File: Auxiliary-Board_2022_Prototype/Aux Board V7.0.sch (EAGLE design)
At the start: 68 parts, among them CON11 1X01, CON12 1X01, CON13 1X01, CON14 1X01, CON15 1X01, CON16 1X01, CON17 1X01, CON18 1X01, CON5 1X01, CON8 1X01, IC1 RS232-TTL_MAX232E

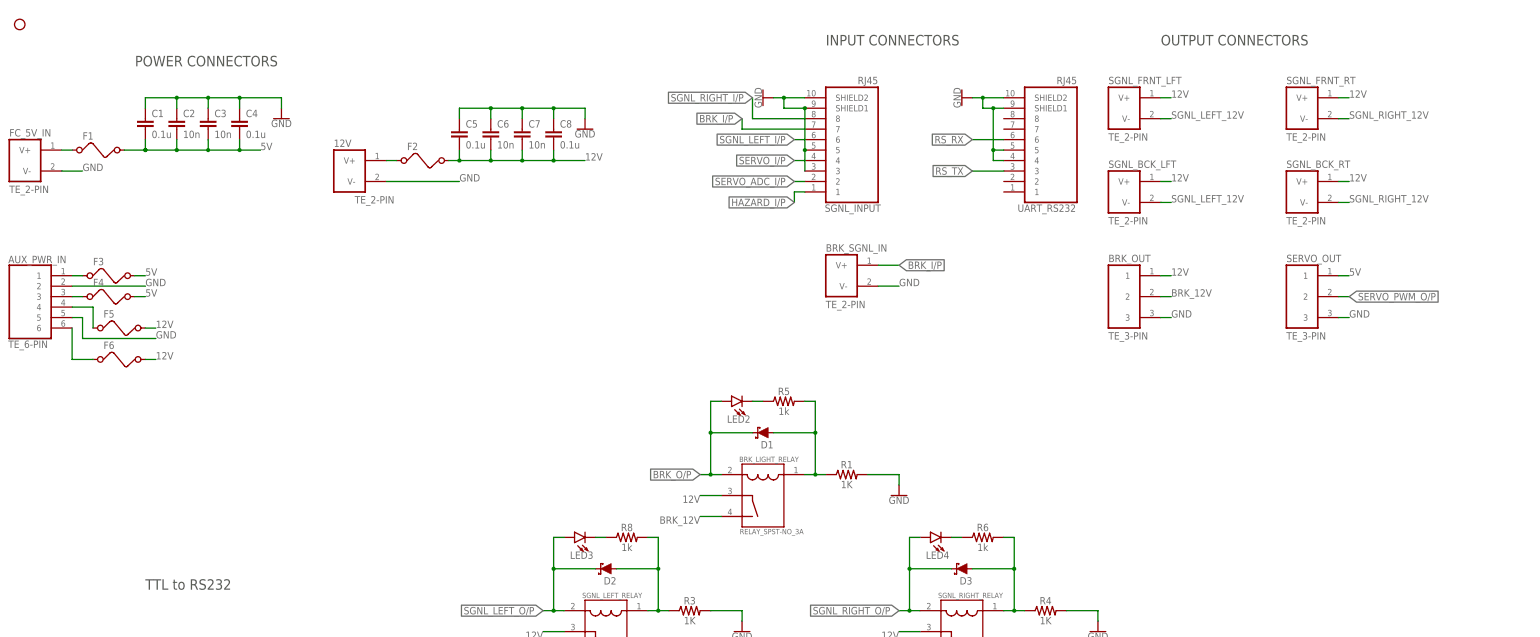
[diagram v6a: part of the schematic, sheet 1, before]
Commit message: feat: connect fuses and power LEDs on board, switch RS232 connector to RJ45 that supports LEDs
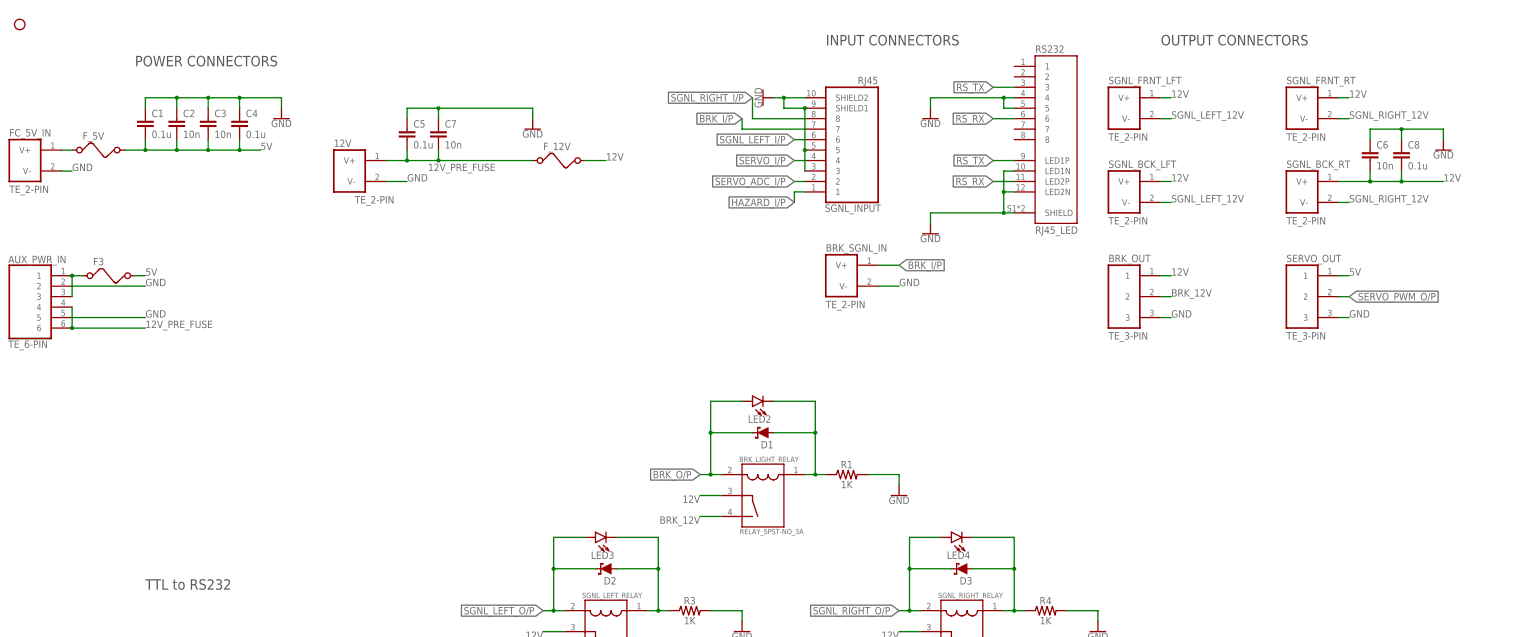
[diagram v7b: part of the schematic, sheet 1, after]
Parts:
- removed F2, F4, F5, F6: (no value), EcoCar-Fuses-Protection:FUSE_1210
- removed R5, R6, R8: 1k, EcoCar-Passives:RESISTOR_0805
- removed UART_RS232: RJ45, EcoCar-Connectors:RJ45
- added F_12V: (no value), EcoCar-Fuses-Protection:FUSE_1210
- added RS232: RJ45_LED, EcoCar-Connectors:RJ45_LED
- renumbered F1 to F_5V
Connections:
- removed net N$30: LED2.C, R5.1
- removed net N$31: LED4.C, R6.1
- removed net N$32: LED3.C, R8.1
- removed net N$35: 12V.V+, F2.1
- removed net N$37: AUX_PWR_IN.3, F4.1
- new net 12V_PRE_FUSE: 12V.V+, AUX_PWR_IN.4, AUX_PWR_IN.6, C5.2, C7.2, F_12V.1
- net 12V: now also F_12V.2; no longer AUX_PWR_IN.4, AUX_PWR_IN.6, C5.2, C7.2, F2.2, F5.1, F5.2, F6.1, F6.2
- net 5V: no longer F4.2
- net GND: now also RS232.4, RS232.5, RS232.LED1N, RS232.LED2N, RS232.SHIELD; no longer UART_RS232.4, UART_RS232.5, UART_RS232.SHIELD1, UART_RS232.SHIELD2
- net N$1: now also LED2.C; no longer R5.2
- net N$13: now also LED3.C; no longer R8.2
- net N$14: now also LED4.C; no longer R6.2
- net N$36: now also AUX_PWR_IN.3
- net RS_RX: now also RS232.6, RS232.LED2P; no longer UART_RS232.6
- net RS_TX: now also RS232.3, RS232.LED1P; no longer UART_RS232.3
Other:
- moved on the sheet: C5, C6, C7, C8, LED2, LED3, LED4

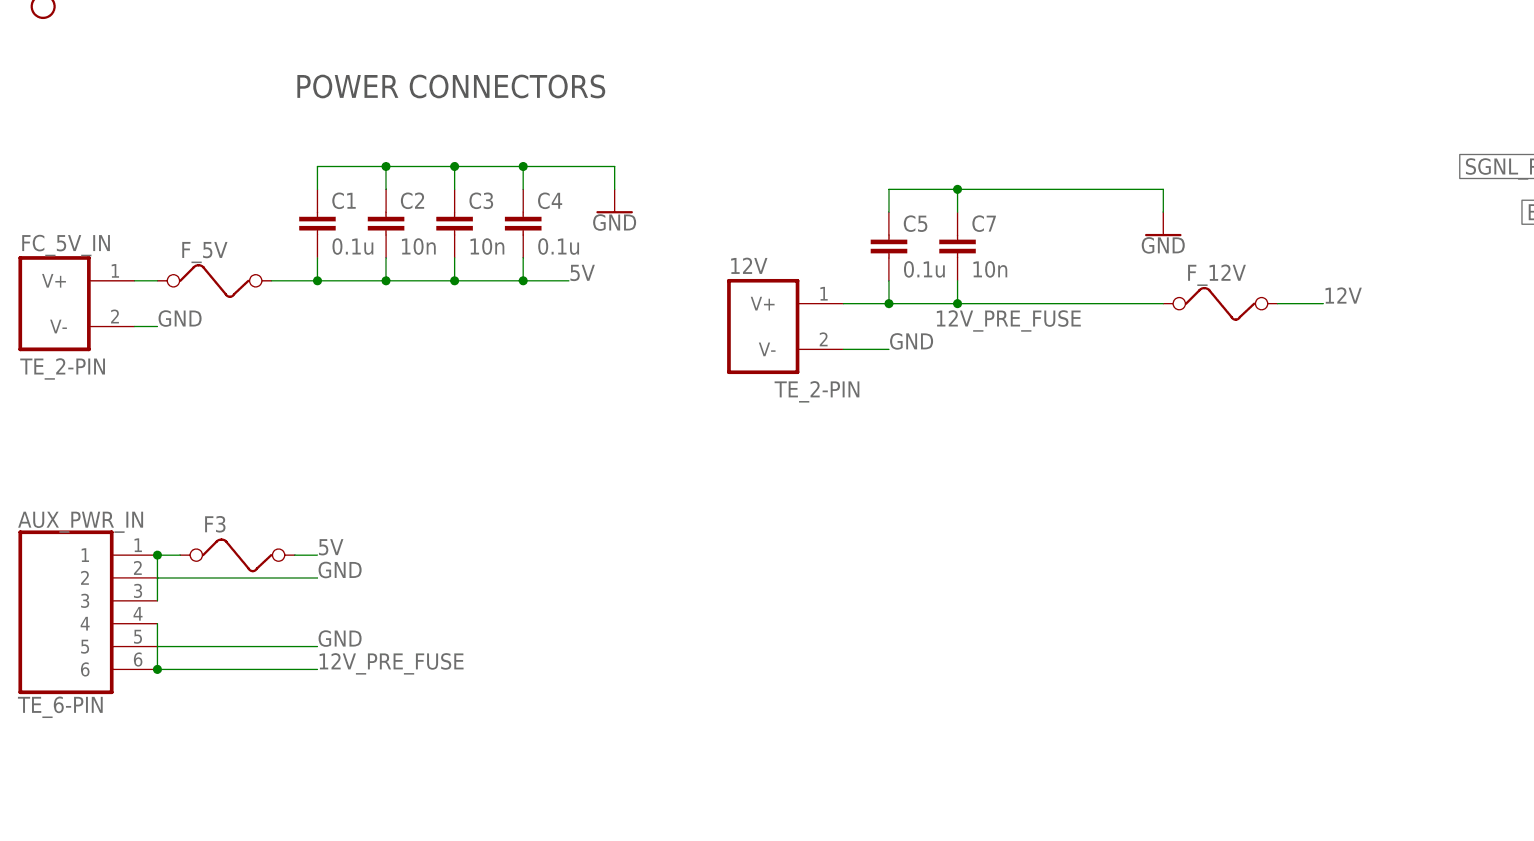
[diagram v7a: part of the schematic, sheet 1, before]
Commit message: feat: finalize V7.0, remove fuses and change jumper
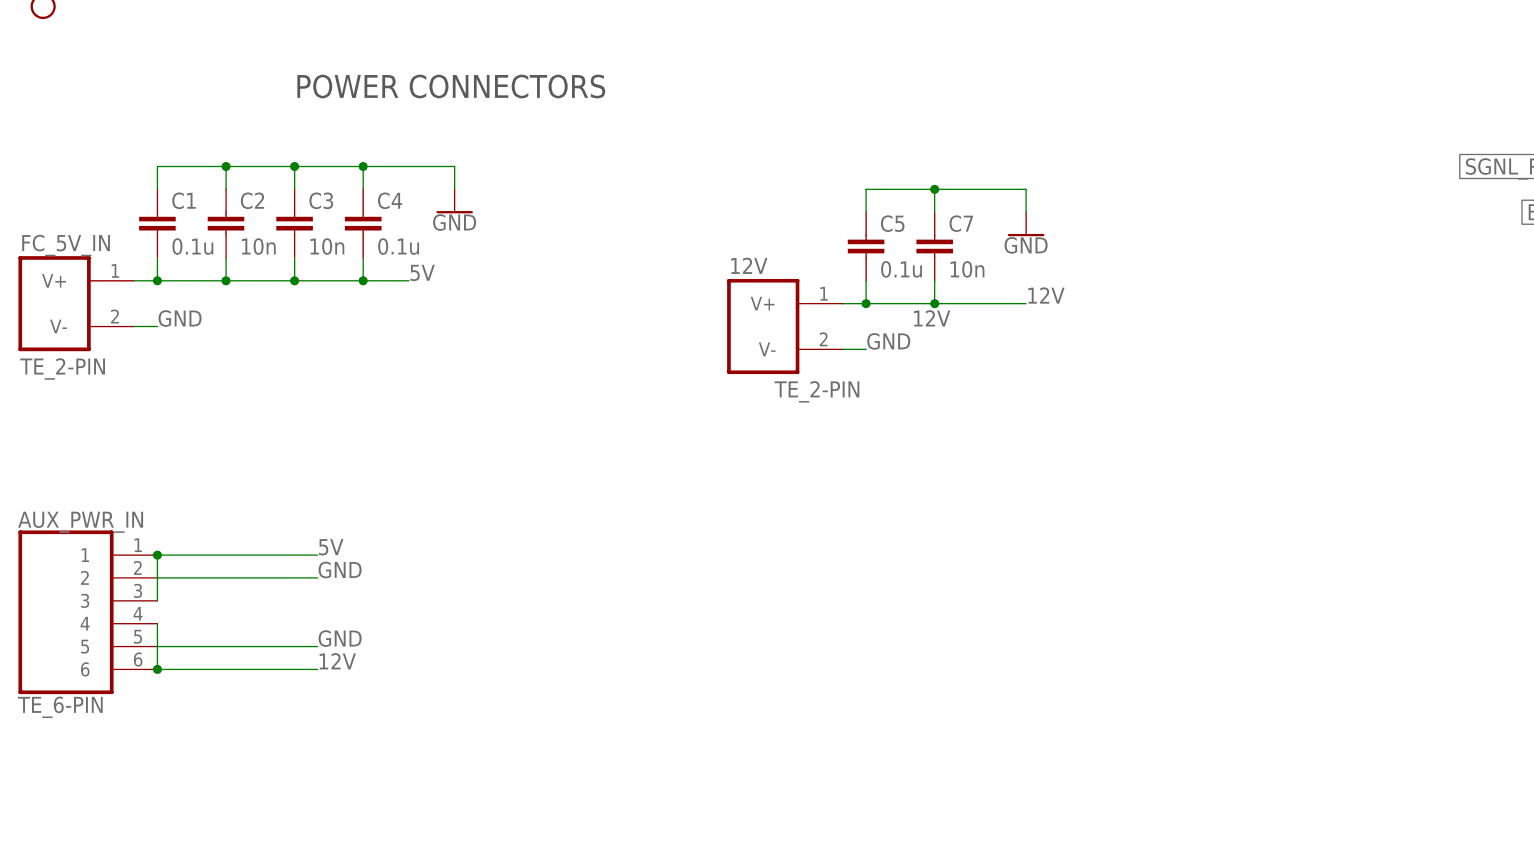
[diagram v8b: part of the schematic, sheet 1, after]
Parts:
- removed AVCC_JMP: (no value), EcoCar-Passives:JUMPER-0.45
- removed F3, F_12V, F_5V: (no value), EcoCar-Fuses-Protection:FUSE_1210
- added AVCC_JUMP: 1X02, EcoCar-Connectors-2.54mm:1X02
- added C15: 10n, EcoCar-Passives:CAPACITOR_0805
- R2: value 2K -> 1K
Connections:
- removed net 12V_PRE_FUSE: 12V.V+, AUX_PWR_IN.4, AUX_PWR_IN.6, C5.2, C7.2, F_12V.1
- removed net N$2: AVCC_JMP.2, MCU_328P2.AVCC
- removed net N$33: FC_5V_IN.V+, F_5V.1
- removed net N$36: AUX_PWR_IN.1, AUX_PWR_IN.3, F3.1
- new net AREF: C15.1, MCU_328P2.AREF
- new net AVCC_5V: AVCC_JUMP.1, MCU_328P2.AVCC
- net 12V: now also 12V.V+, AUX_PWR_IN.4, AUX_PWR_IN.6, C5.2, C7.2; no longer F_12V.2
- net 5V: now also AUX_PWR_IN.1, AUX_PWR_IN.3, AVCC_JUMP.2, FC_5V_IN.V+; no longer AVCC_JMP.1, F3.2, F_5V.2
- net GND: now also C15.2
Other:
- moved on the sheet: C1, C2, C3, C4, C5, C7, LED1, R2
